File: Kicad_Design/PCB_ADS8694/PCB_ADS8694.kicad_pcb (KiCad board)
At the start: 2 copper layers, 46 parts, among them J1 Screw_Terminal_01x03_Alimenta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, J4 Conn_02x06_Male_Pmod_Spartan6, J5 Screw_Terminal_01x02_CH3, J6 Screw_Terminal_01x02_CH2, J7 Screw_Terminal_01x02_CH1, J8 Screw_Terminal_01x02_CH0, U1 LM7805_TO220, U2 AD8221, U3 AD8221, U4 ADS8694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

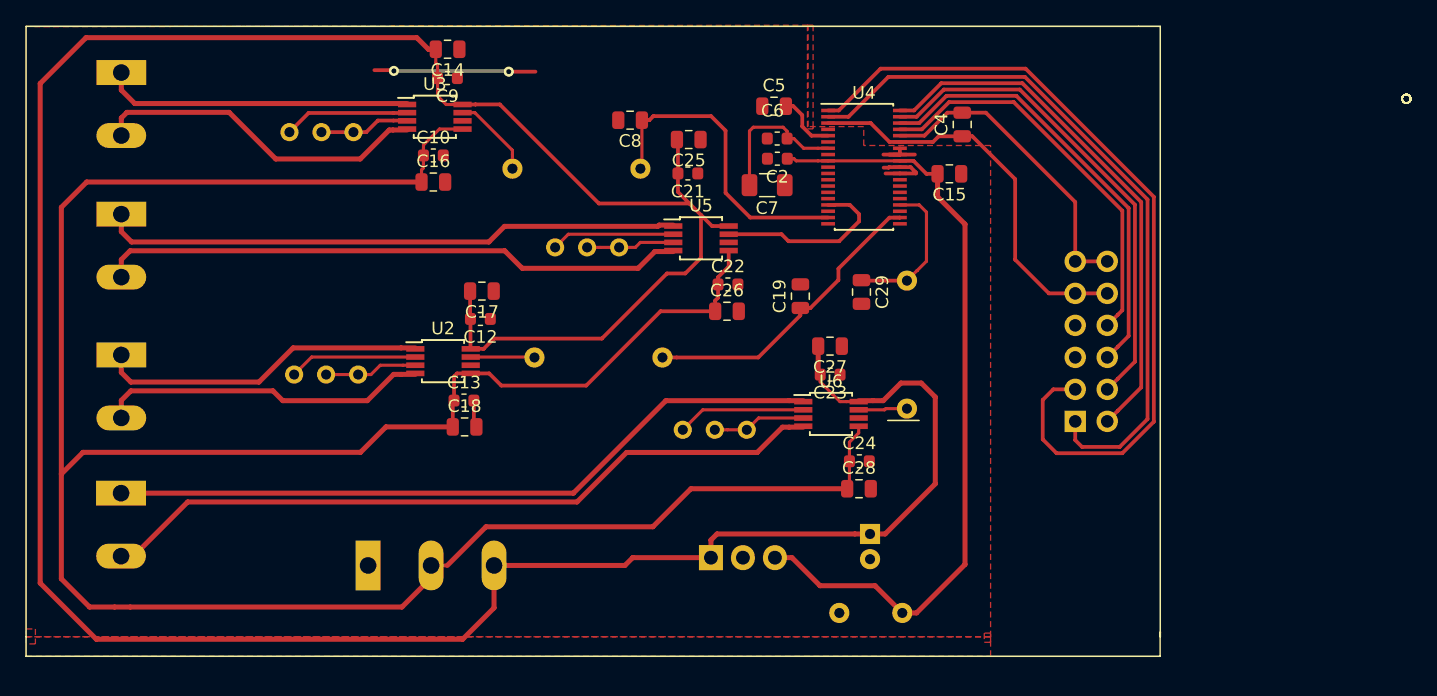
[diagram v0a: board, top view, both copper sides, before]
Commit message: Cambios en encapsulados. Agregado de serigrafía
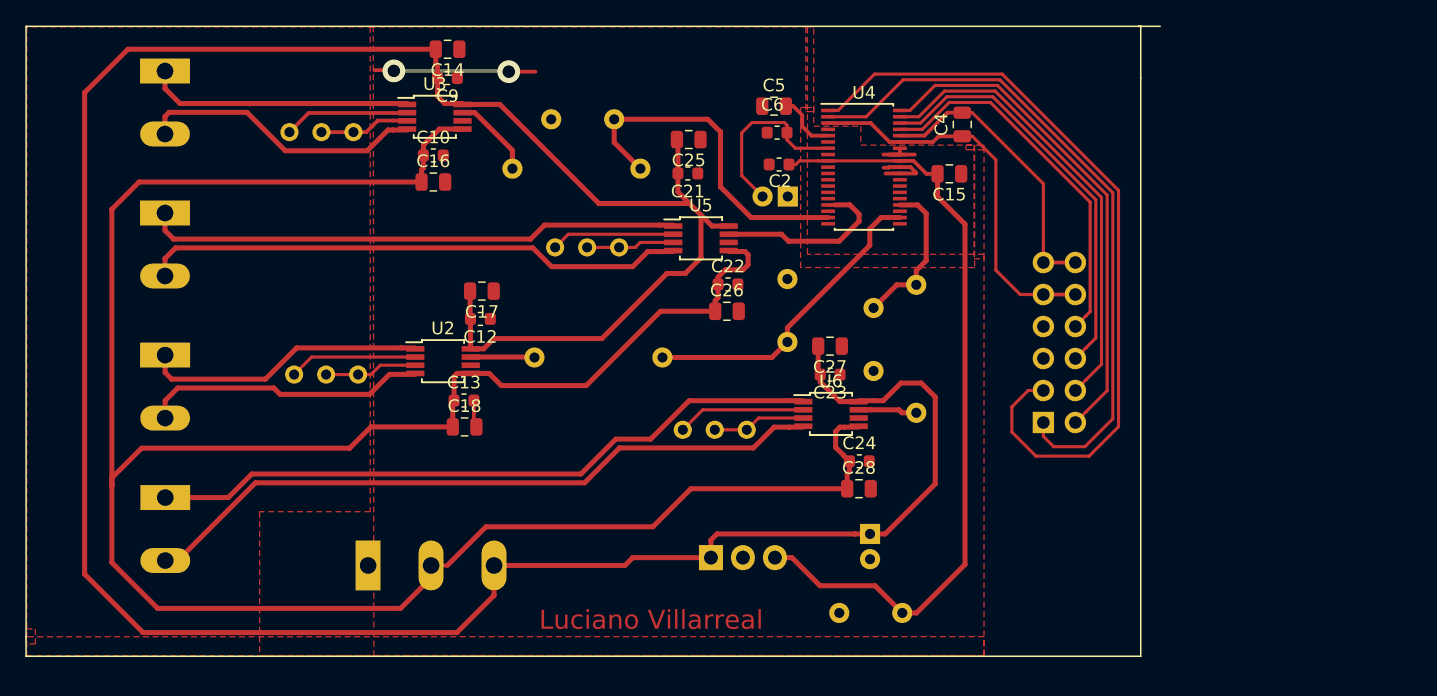
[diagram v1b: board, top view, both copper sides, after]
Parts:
- C19, C29, C8: footprint Capacitor_SMD:C_0805_2012Metric -> Capacitor_THT:C_Disc_D5.0mm_W2.5mm_P5.00mm; moved to B.Cu
- C7: footprint Capacitor_SMD:C_1206_3216Metric -> Capacitor_THT:CP_Radial_D5.0mm_P2.00mm; moved to B.Cu
- moved C19 3.78 mm to (176.9, 106.1)
- moved J5 3.53 mm to (127.5, 118.5)
- moved J6 3.48 mm to (127.5, 107.2)
- moved J7 3.47 mm to (127.5, 84.6)
- moved J8 3.47 mm to (127.5, 95.9)
- moved J4 2.53 mm to (197.2, 112.5)
- moved C7 1.87 mm to (176.9, 94.6)
- moved C29 1.59 mm to (183.8, 103.4)
- moved C8 1.26 mm to (163.2, 88.5)
- moved R3 0.81 mm to (187.2, 101.6)
- moved C2 0.48 mm to (176.3, 92.0)
- moved C6 0.47 mm to (176.1, 89.5)
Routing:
- net VCC: track 240.3 -> 230.6 mm
- net VSS: track 204.3 -> 196.7 mm
- net AIN_1+: track 26.8 -> 22.7 mm
- net AIN_2+: track 26.2 -> 22.5 mm
- net AIN_2-: track 26.2 -> 22.5 mm
- net AIN_0-: track 46.1 -> 42.5 mm
- net SDI: track 65.7 -> 62.1 mm
- net AIN_0+: track 46.6 -> 43.2 mm
- net AIN_1-: track 24.5 -> 21.1 mm
- net AIN_3+: track 58.4 -> 55.0 mm
- net AIN_3-: track 57.2 -> 53.8 mm
- net RST-PD: track 56.5 -> 53.4 mm
- net REFCAP: track 11.7 -> 14.5 mm
- net CS: track 42.5 -> 40.0 mm
- net AIN_1P: track 25.0 -> 27.5 mm
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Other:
- board text added: "+VCC"
- board text added: "-VCC"
- board text added: "4 CANALES DIFERENCIALES ADS8684 COMUNICACIÓN SPI"
- board text added: "CH 0"
- board text added: "CH 1"
- board text added: "CH0"
- board text added: "CH1"
- board text added: "CH2"
- board text added: "CH3"
- board text added: "GND"
- board text added: "GND GND"
- board text added: "Luciano Villarreal"
- board text added: "NC ALARM"
- board text added: "NC SDO"
- board text added: "RST-PD CS"
- board text added: "SDI SCLK"
- board text added: "VDD VDD"

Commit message: cambios varios, reduccion de tamaño
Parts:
- moved C8 6.41 mm to (169.2, 86.2)
- moved R2 6.16 mm to (173.2, 107.5)
- moved C12 5.79 mm to (158.3, 104.9)
- moved C13 5.79 mm to (157.0, 111.4)
- moved C17 5.79 mm to (158.4, 102.7)
- moved C18 5.79 mm to (157.0, 113.5)
- moved RV2 5.79 mm to (143.5, 109.4)
- moved U2 5.79 mm to (155.3, 108.3)
- moved J1 3.71 mm to (147.3, 123.4)
- moved C1 3.49 mm to (181.4, 124.2), turned to 90 degrees
- moved RV1 2.95 mm to (140.3, 89.5)
- moved C14 2.95 mm to (152.9, 83.0)
- moved C10 2.95 mm to (151.8, 91.4)
- moved C16 2.95 mm to (151.8, 93.5)
- moved C9 2.95 mm to (152.9, 85.2)
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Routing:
- net VSS: track 196.7 -> 189.8 mm
- net AIN_2P: track 24.9 -> 18.6 mm
- net VCC: track 230.6 -> 226.6 mm
- net AIN_0+: track 43.2 -> 39.5 mm
- net AIN_1+: track 22.7 -> 20.3 mm
- net AIN_0-: track 42.5 -> 40.2 mm
- net AIN_2+: track 22.5 -> 24.8 mm
- net AIN_3-: track 53.8 -> 51.8 mm
- net AIN_1P: track 27.5 -> 25.5 mm
- net AIN_3+: track 55.0 -> 53.0 mm
- net Net-(R3-Pad2): track 4.67 -> 6.65 mm
- net REFSEL: track 24.1 -> 25.6 mm
- net AVDD: track 62.8 -> 64.2 mm
- net AIN_2-: track 22.5 -> 23.5 mm
- net Net-(R1-Pad2): track 6.66 -> 7.38 mm
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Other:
- board text added: "+"
- board text added: "-"
- board text added: "4 CANALES DIFERENCIALES ADS8694 COMUNICACIÓN SPI"
- board text removed: "4 CANALES DIFERENCIALES ADS8684 COMUNICACIÓN SPI"
- board text removed: "CH 0"
- board text removed: "CH 1"
